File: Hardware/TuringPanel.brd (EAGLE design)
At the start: 107 x 49.5 mm, 0 parts

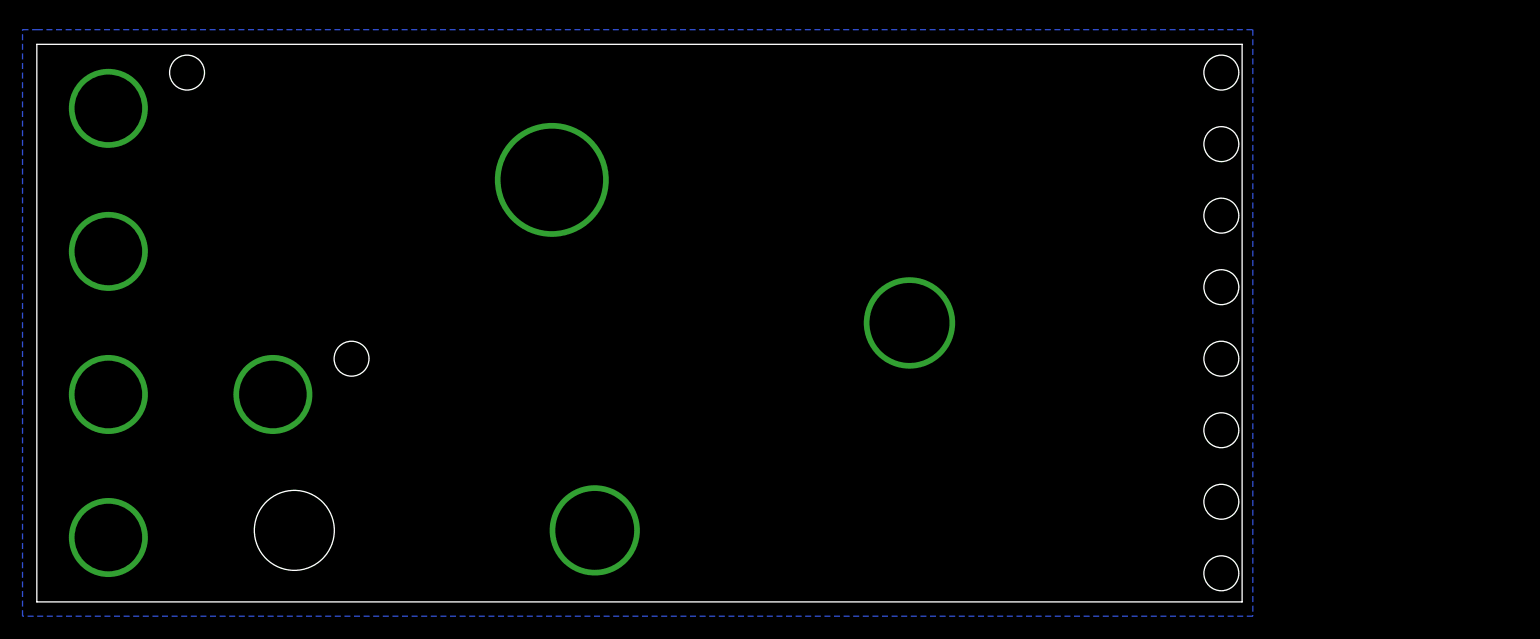
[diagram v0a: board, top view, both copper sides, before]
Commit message: fix sizing and add mounting holes
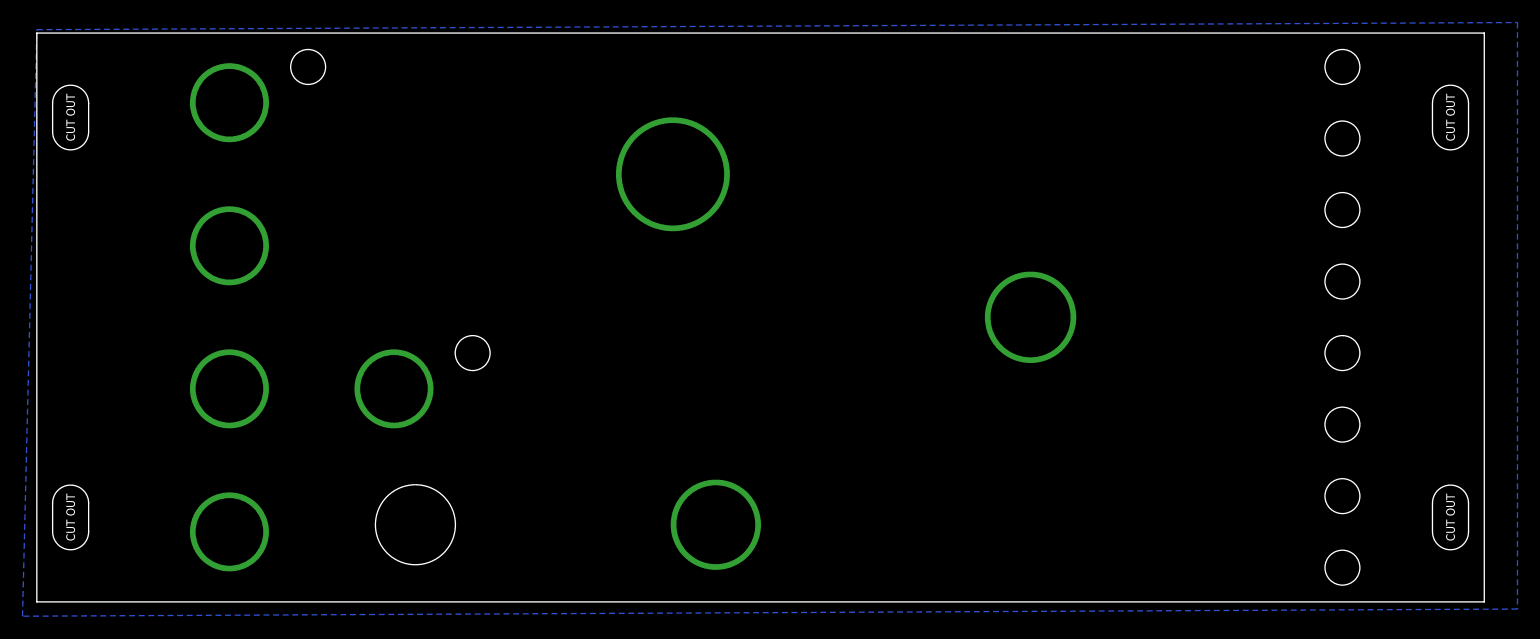
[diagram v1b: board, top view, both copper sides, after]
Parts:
- added U$1, U$2, U$3, U$4: (no value), MusicThingModular:SLOT_HOLE
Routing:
- added copper zone on layer 16, net GND
- removed copper zone on layer 16, net GND_FRONT
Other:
- board size 107 x 49.5 mm -> 128.5 x 50.5 mm
- board text added: "Music Thing Modular Turing Machine Panel Prototype 1 September 2015 CC-BY-SA"
- board text removed: "Music Thing Modular Turing Machine Rev 4 Prototype 2 July 2015 CC-BY-SA"
